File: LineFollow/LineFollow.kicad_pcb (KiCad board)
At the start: 2 copper layers, 28 x 24 mm, 12 parts, among them P1 CONN_01X04, U1 LEFT_SENSE, U2 RIGHT_SENSE

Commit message: Updated for version 2.0f
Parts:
- P1: moved to F.Cu
- R1, R3: value 220 -> 160
- turned LED1 to 270 degrees
- turned LED2 to 270 degrees
- turned P1 to 90 degrees
- turned U1 to 270 degrees
- turned U2 to 270 degrees
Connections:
- LED1 pad 1: Net-(LED1-Pad1) -> GND
- LED1 pad 2: GND -> Net-(LED1-Pad2)
- LED2 pad 1: Net-(LED2-Pad1) -> GND
- LED2 pad 2: GND -> Net-(LED2-Pad2)
- R1 pad 1: Net-(LED1-Pad1) -> Net-(LED1-Pad2)
- R3 pad 1: Net-(LED2-Pad1) -> Net-(LED2-Pad2)
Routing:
- net Net-(LED1-Pad2): track 0.00 -> 17.5 mm
- net Net-(LED1-Pad1): track 17.5 -> 0.00 mm
- net Net-(LED2-Pad2): track 0.00 -> 14.5 mm
- net Net-(LED2-Pad1): track 14.2 -> 0.00 mm
- net Net-(P1-Pad4): track 27.1 -> 25.2 mm
- net Net-(P1-Pad3): track 22.6 -> 24.0 mm
- net GND: track 11.6 -> 12.1 mm
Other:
- board text added: "Mirobot Line Follower v1.2 © Ben Pirt 2015"
- board text removed: "Mirobot Line Follower v1.1 © Ben Pirt 2015"

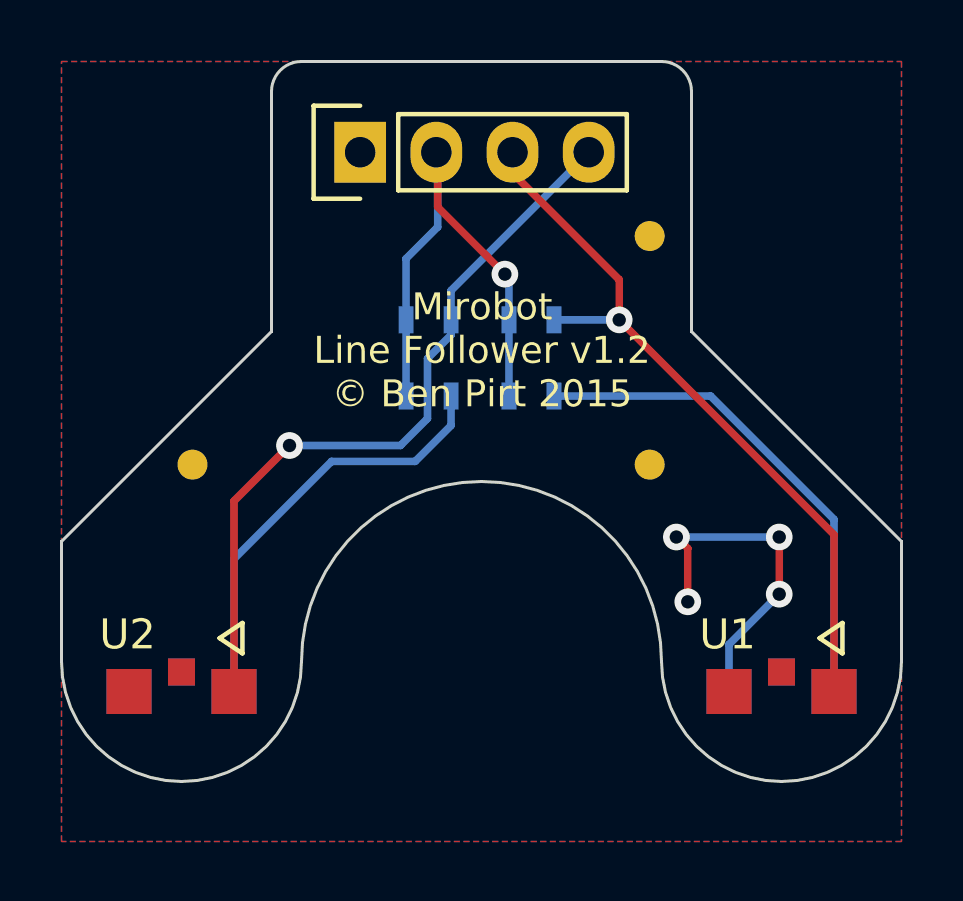
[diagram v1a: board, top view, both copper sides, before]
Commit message: Switch the phototransistor around so that it works with the in stock parts
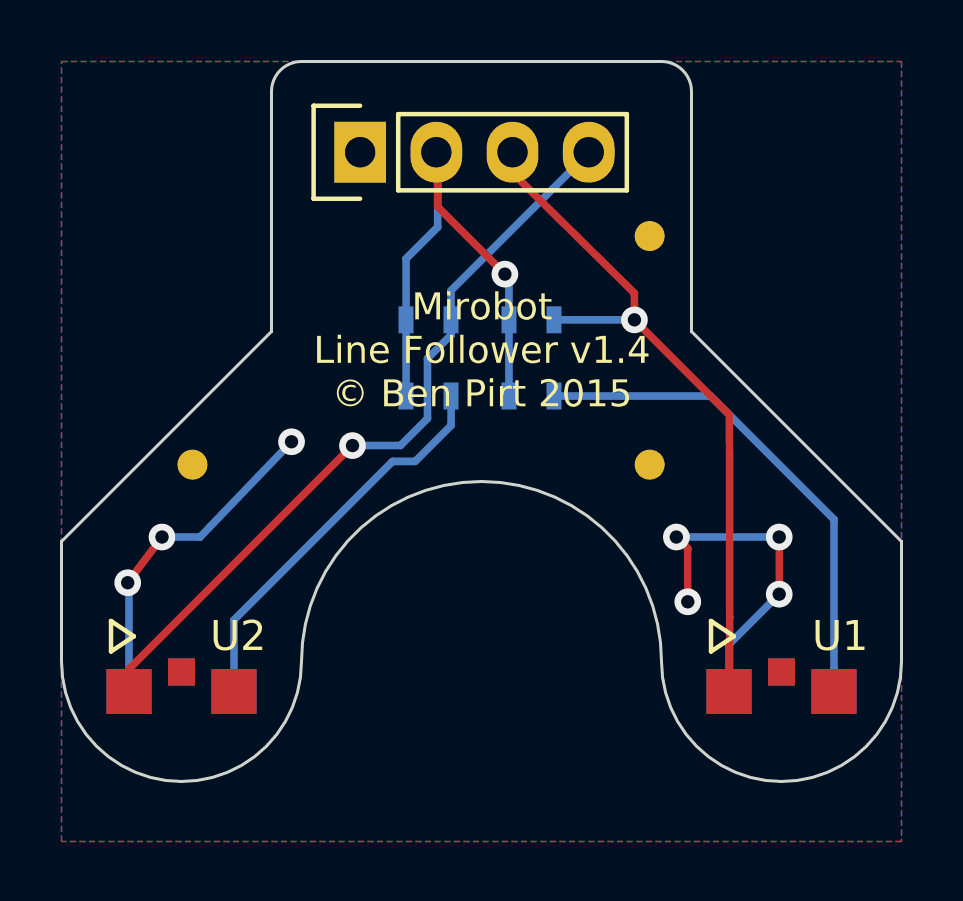
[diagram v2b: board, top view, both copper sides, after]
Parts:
- U1, U2: footprint Mirobot:SIDE-LED -> Mirobot:SIDE-LED-REVERSED
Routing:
- net GND: track 12.1 -> 22.8 mm, vias 4 -> 7
- net Net-(LED2-Pad2): track 14.5 -> 13.3 mm
- net Net-(P1-Pad3): track 24.0 -> 23.1 mm
- net Net-(P1-Pad4): track 25.2 -> 25.9 mm
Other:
- board text added: "Mirobot Line Follower v1.4 © Ben Pirt 2015"
- board text removed: "Mirobot Line Follower v1.2 © Ben Pirt 2015"
